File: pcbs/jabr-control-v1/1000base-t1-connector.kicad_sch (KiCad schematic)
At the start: 1 part, among them J8001 MSPE-J2L0-x00

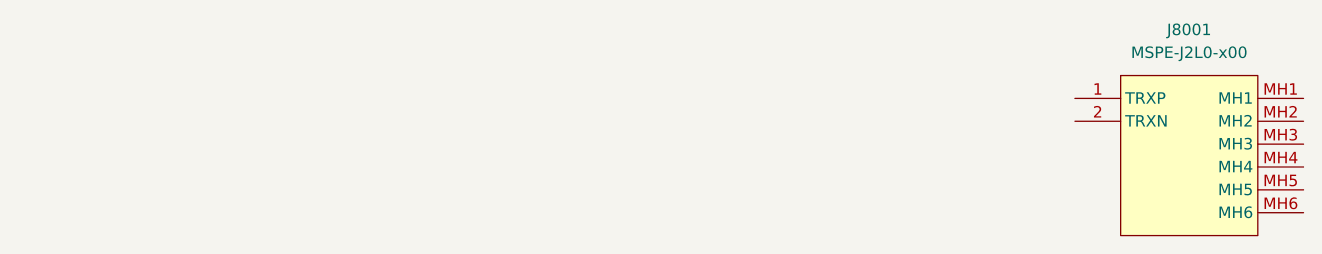
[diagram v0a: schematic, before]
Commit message: Added PCIe connections
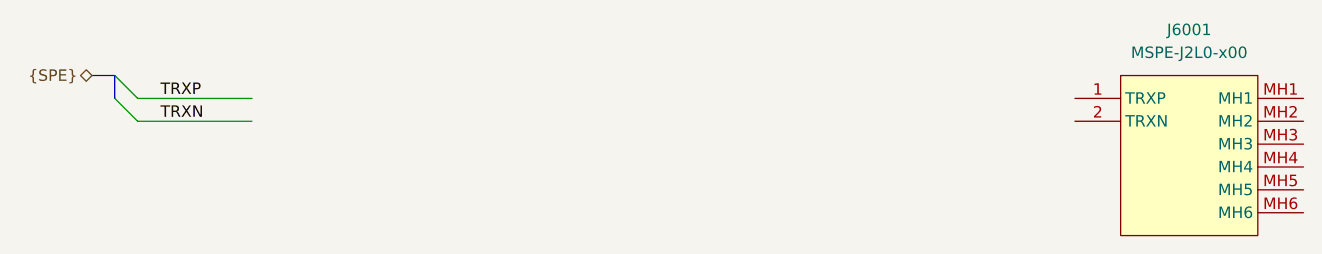
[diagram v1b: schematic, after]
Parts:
- renumbered J8001 to J6001
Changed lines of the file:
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@@
 	(generator_version "9.0")
 	(paper "A4")
+	(bus_entry
+		(at 88.9 71.12)
+		(size 2.54 2.54)
+		(stroke
+			(width 0)
+			(type default)
+		)
+	)
+	(bus_entry
+		(at 88.9 68.58)
+		(size 2.54 2.54)
+		(stroke
+			(width 0)
+			(type default)
+		)
+	)
+	(wire
+		(pts
+			(xy 91.44 71.12) (xy 104.14 71.12)
+		)
+		(stroke
+			(width 0)
+			(type default)
+		)
+	)
+	(bus
+		(pts
+			(xy 88.9 68.58) (xy 88.9 71.12)
+		)
+		(stroke
+			(width 0)
+			(type default)
+		)
+	)
+	(bus
+		(pts
+			(xy 86.36 68.58) (xy 88.9 68.58)
+		)
+		(stroke
+			(width 0)
+			(type default)
+		)
+	)
+	(wire
+		(pts
+			(xy 91.44 73.66) (xy 104.14 73.66)
+		)
+		(stroke
+			(width 0)
+			(type default)
+		)
+	)
+	(label "TRXN"
+		(at 93.98 73.66 0)
+		(effects
+			(font
+				(size 1.27 1.27)
+			)
+			(justify left bottom)
+		)
+	)
+	(label "TRXP"
+		(at 93.98 71.12 0)
+		(effects
+			(font
+				(size 1.27 1.27)
+			)
+			(justify left bottom)
+		)
+	)
+	(hierarchical_label "{SPE}"
+		(shape bidirectional)
+		(at 86.36 68.58 180)
+		(effects
+			(font
+				(size 1.27 1.27)
+			)
+			(justify right)
+		)
+	)
 	(symbol
 		(lib_id "ETH-CONN:MSPE-J2L0-x00")
@@
 		(dnp no)
 		(fields_autoplaced yes)
-		(property "Reference" "J8001"
+		(property "Reference" "J6001"
 			(at 208.28 63.5 0)
 			(effects
@@
 		)
 		(instances
-			(project ""
-				(path "/f91ec272-d09a-4038-bbbb-962739a92c51/9e4cc40e-1b85-46ff-be45-c4800a75e0fe"
-					(reference "J8001")
+			(project "jabr-control-v1"
+				(path "/f91ec272-d09a-4038-bbbb-962739a92c51/3124e188-7d93-47d9-82c9-cb765ca396d3/ae7374e5-3d79-45a7-a1a6-e5f21fb2a45c"
+					(reference "J6001")
 					(unit 1)
 				)

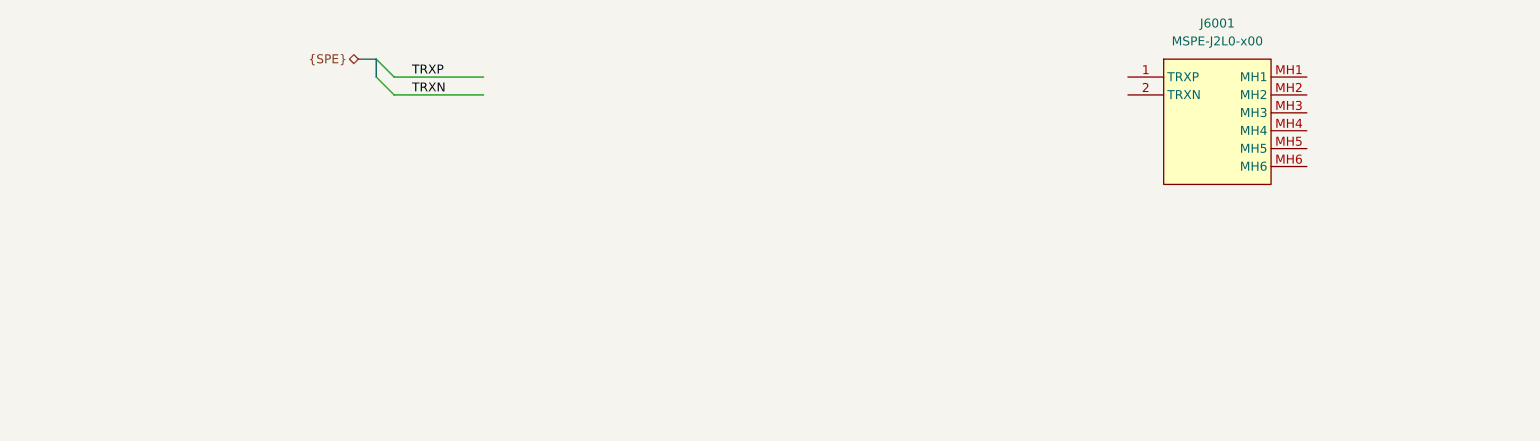
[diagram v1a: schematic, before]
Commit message: Added power sheets
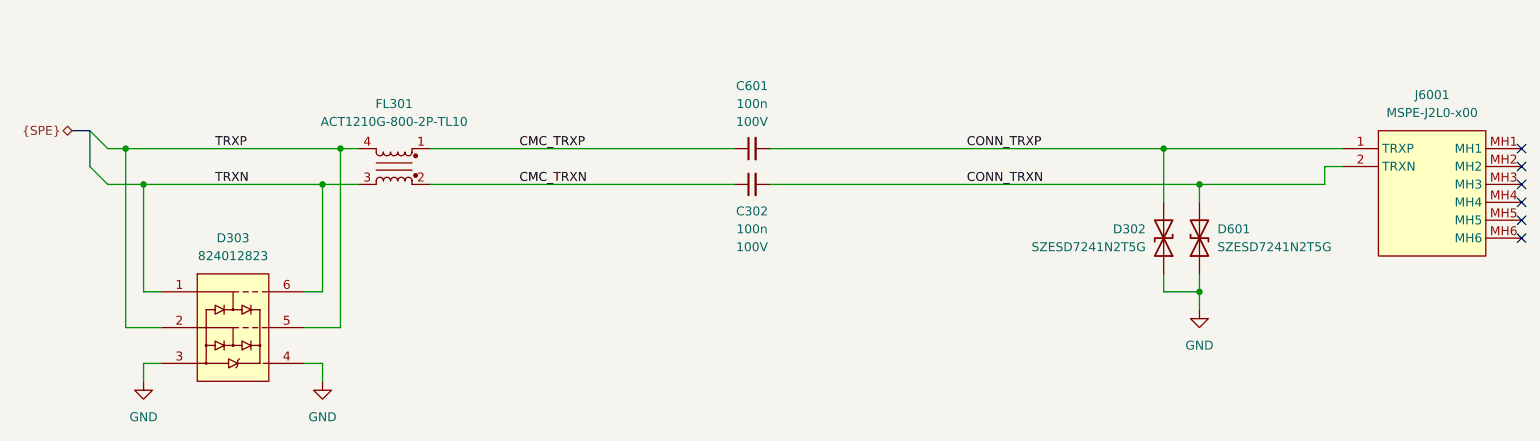
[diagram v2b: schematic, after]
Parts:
- added C302, C601: 100n, Capacitor_SMD:C_0603_1608Metric, symbol Device:C_Small
- added D302, D601: SZESD7241N2T5G, project_footprints:SZESD7462N2T5G, symbol TVS:SZESD7241N2T5G
- added D303: 824012823, project_footprints:824012823, symbol TVS:824012823
- added FL301: ACT1210G-800-2P-TL10, project_footprints:ACT1210G, symbol COMM-CMC:ACT1210G-800-2P-TL10
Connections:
- net TRXN: now also D303.1, D303.6, FL301.3
- net TRXP: now also D303.2, D303.5, FL301.4
- net CONN_TRXP: now reaches J6001.1 (TRXP)
- net CONN_TRXP: now also C601.2, D302.2 (A2)
- net CONN_TRXN: now reaches J6001.2 (TRXN)
- net CONN_TRXN: now also C302.2, D601.2 (A2)
- new net CMC_TRXN: C302.1, FL301.2
- new net CMC_TRXP: C601.1, FL301.1
- new net GND: D302.1 (A1), D303.3, D303.4, D601.1 (A1)
- no-connect marks 0 -> 6
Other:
- moved on the sheet: J6001

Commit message: Schematic nearing completion, need to do GPIO and PHY decouplings caps
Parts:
- C302, C601: footprint Capacitor_SMD:C_0603_1608Metric -> project_footprints:C_0603; symbol Device:C_Small -> DEV:C_SMALL
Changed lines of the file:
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@@
 	)
 	(symbol
-		(lib_id "Device:C_Small")
+		(lib_id "DEV:C_SMALL")
 		(at 142.24 86.36 90)
 		(unit 1)
@@
 			)
 		)
-		(property "Footprint" "Capacitor_SMD:C_0603_1608Metric"
+		(property "Footprint" "project_footprints:C_0603"
 			(at 142.24 86.36 0)
 			(effects
@@
 					(size 1.27 1.27)
 				)
+			)
+		)
+		(property "Field6" ""
+			(at 142.24 86.36 90)
+			(effects
+				(font
+					(size 1.27 1.27)
+				)
+				(hide yes)
+			)
+		)
+		(property "Field7" ""
+			(at 142.24 86.36 90)
+			(effects
+				(font
+					(size 1.27 1.27)
+				)
+				(hide yes)
+			)
+		)
+		(property "Part Description" ""
+			(at 142.24 86.36 90)
+			(effects
+				(font
+					(size 1.27 1.27)
+				)
+				(hide yes)
 			)
 		)
@@
 			)
 		)
+		(property "Field6" ""
+			(at 205.74 93.98 90)
+			(effects
+				(font
+					(size 1.27 1.27)
+				)
+				(hide yes)
+			)
+		)
+		(property "Field7" ""
+			(at 205.74 93.98 90)
+			(effects
+				(font
+					(size 1.27 1.27)
+				)
+				(hide yes)
+			)
+		)
+		(property "Part Description" ""
+			(at 205.74 93.98 90)
+			(effects
+				(font
+					(size 1.27 1.27)
+				)
+				(hide yes)
+			)
+		)
 		(pin "2"
 		)
@@
 			)
 		)
+		(property "Field6" ""
+			(at 91.44 81.28 0)
+			(effects
+				(font
+					(size 1.27 1.27)
+				)
+				(hide yes)
+			)
+		)
+		(property "Field7" ""
+			(at 91.44 81.28 0)
+			(effects
+				(font
+					(size 1.27 1.27)
+				)
+				(hide yes)
+			)
+		)
+		(property "Part Description" ""
+			(at 91.44 81.28 0)
+			(effects
+				(font
+					(size 1.27 1.27)
+				)
+				(hide yes)
+			)
+		)
 		(pin "1"
 		)
@@
 			)
 		)
+		(property "Field6" ""
+			(at 238.76 78.74 0)
+			(effects
+				(font
+					(size 1.27 1.27)
+				)
+				(hide yes)
+			)
+		)
+		(property "Field7" ""
+			(at 238.76 78.74 0)
+			(effects
+				(font
+					(size 1.27 1.27)
+				)
+				(hide yes)
+			)
+		)
+		(property "Part Description" ""
+			(at 238.76 78.74 0)
+			(effects
+				(font
+					(size 1.27 1.27)
+				)
+				(hide yes)
+			)
+		)
 		(pin "MH3"
 		)
@@
 	)
 	(symbol
-		(lib_id "Device:C_Small")
+		(lib_id "DEV:C_SMALL")
 		(at 142.24 81.28 90)
 		(mirror x)
@@
 			)
 		)
-		(property "Footprint" "Capacitor_SMD:C_0603_1608Metric"
+		(property "Footprint" "project_footprints:C_0603"
 			(at 142.24 81.28 0)
 			(effects
@@
 					(size 1.27 1.27)
 				)
+			)
+		)
+		(property "Field6" ""
+			(at 142.24 81.28 90)
+			(effects
+				(font
+					(size 1.27 1.27)
+				)
+				(hide yes)
+			)
+		)
+		(property "Field7" ""
+			(at 142.24 81.28 90)
+			(effects
+				(font
+					(size 1.27 1.27)
+				)
+				(hide yes)
+			)
+		)
+		(property "Part Description" ""
+			(at 142.24 81.28 90)
+			(effects
+				(font
+					(size 1.27 1.27)
+				)
+				(hide yes)
 			)
 		)
@@
 			)
 		)
+		(property "Field6" ""
+			(at 200.66 93.98 90)
+			(effects
+				(font
+					(size 1.27 1.27)
+				)
+				(hide yes)
+			)
+		)
+		(property "Field7" ""
+			(at 200.66 93.98 90)
+			(effects
+				(font
+					(size 1.27 1.27)
+				)
+				(hide yes)
+			)
+		)
+		(property "Part Description" ""
+			(at 200.66 93.98 90)
+			(effects
+				(font
+					(size 1.27 1.27)
+				)
+				(hide yes)
+			)
+		)
 		(pin "2"
 		)
@@
 				(hide yes)
 			)
+		)
+		(property "Field6" ""
+			(at 68.58 99.06 0)
+			(effects
+				(font
+					(size 1.27 1.27)
+				)
+				(hide yes)
+			)
+		)
+		(property "Field7" ""
+			(at 68.58 99.06 0)
+			(effects
+				(font
+					(size 1.27 1.27)
+				)
+				(hide yes)
+			)
+		)
+		(property "Part Description" ""
+			(at 68.58 99.06 0)
+			(effects
+				(font
+					(size 1.27 1.27)
+				)
+				(hide yes)
+			)
